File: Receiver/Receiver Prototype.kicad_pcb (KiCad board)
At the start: 4 copper layers, 145 x 50.8 mm, 108 parts, among them J1 Conn_01x02_Socket, J10 Conn_01x01, J11 Conn_Coaxial, J12 Conn_Coaxial, J13 Conn_Coaxial, J14 Conn_Coaxial, J15 Conn_01x01, J16 Conn_01x01, J17 Conn_01x02, J18 Conn_01x02, J19 Conn_01x01, J2 Conn_01x01, J20 Conn_01x01, J21 Conn_01x01, J22 Conn_01x01, J23 Conn_01x02, J24 Conn_01x02, J25 Conn_01x01, J26 Conn_01x03, J27 Conn_01x03, J28 Conn_01x02, J29 Conn_01x03, J3 Conn_01x01, J30 Conn_01x03, J4 Conn_Coaxial, J5 Conn_01x01, J6 Conn_01x02, J7 Conn_Coaxial, J8 Conn_Coaxial, J9 Conn_01x01, U1 OPA3692ID, U2 AD8692ARZ, U3 OPA692IDBVR, U4 LT3045EMSE-PBF, U5 AD607ARSZ, U6 LT3094EMSE-PBF

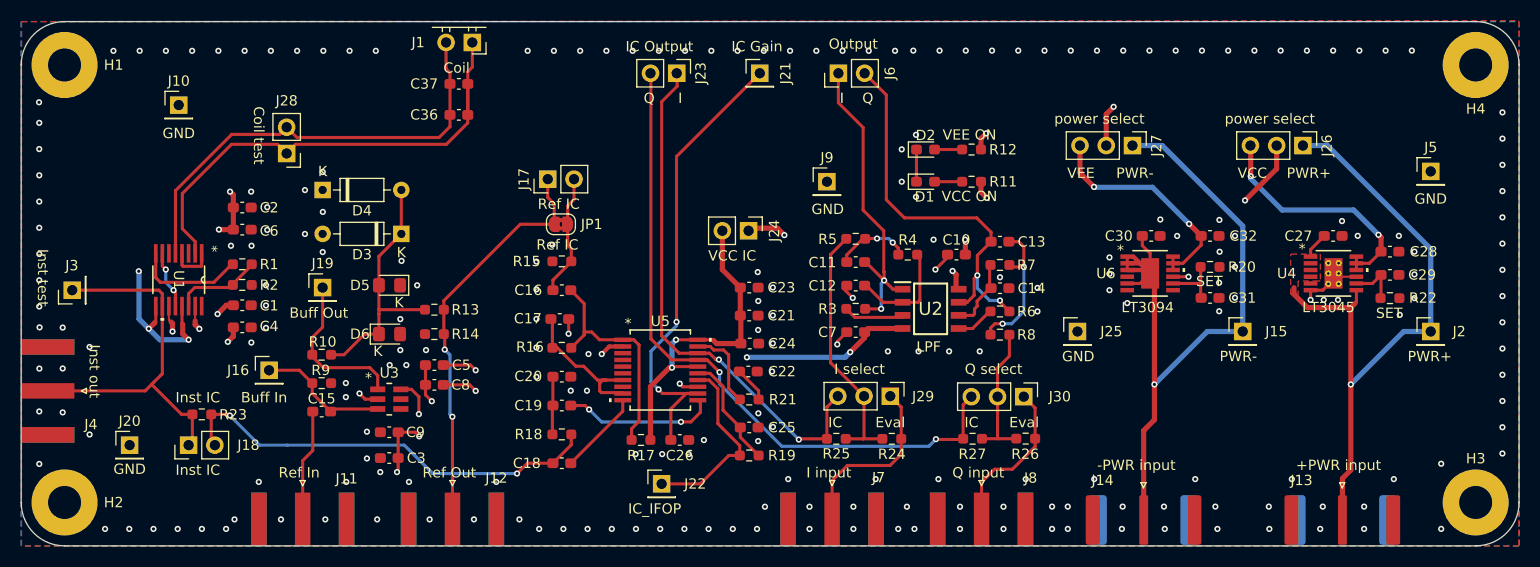
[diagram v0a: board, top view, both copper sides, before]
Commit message: Changed the Receiver layout as discussed on DR3
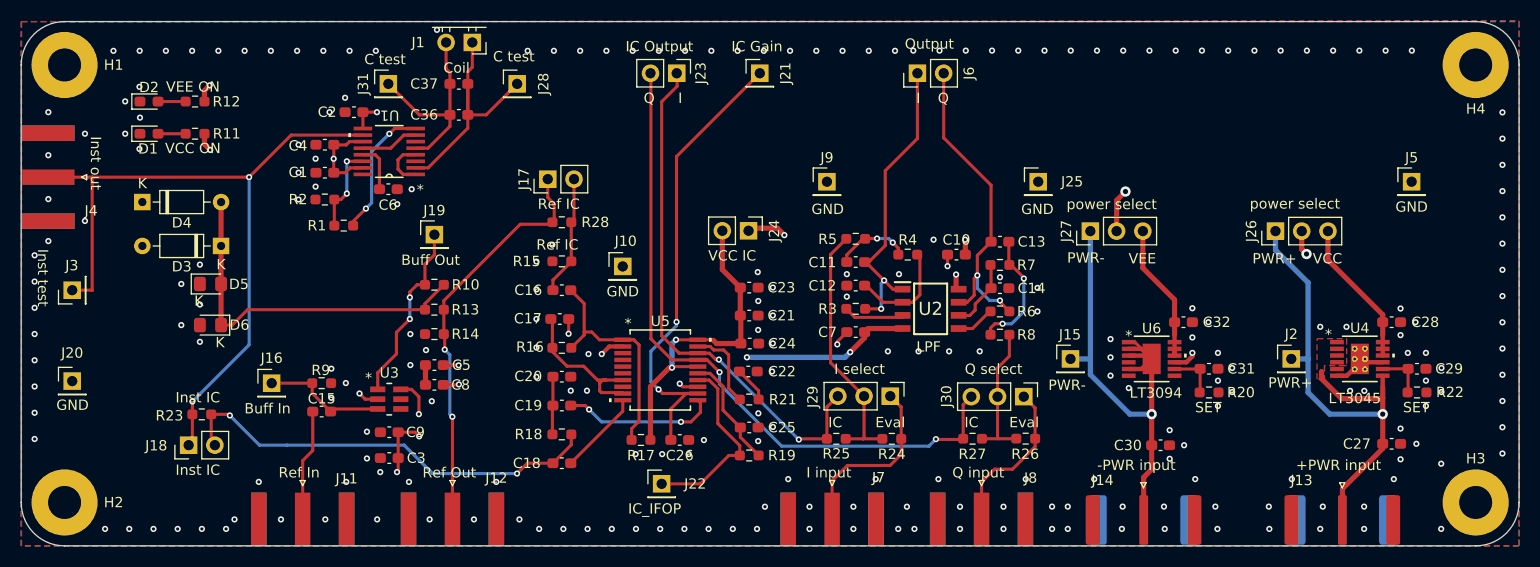
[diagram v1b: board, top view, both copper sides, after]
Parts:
- removed JP1: Jumper_2_Bridged, Jumper:SolderJumper-2_P1.3mm_Bridged2Bar_RoundedPad1.0x1.5mm
- added J31: Conn_01x01, Connector_PinHeader_2.54mm:PinHeader_1x01_P2.54mm_Vertical, F.Cu at (122.3, 56.0)
- added R28: R, Resistor_SMD:R_0603_1608Metric_Pad0.98x0.95mm_HandSolder, F.Cu at (139.1, 69.4)
- J28: value Conn_01x02 -> Conn_01x01; footprint Connector_PinHeader_2.54mm:PinHeader_1x02_P2.54mm_Vertical -> Connector_PinHeader_2.54mm:PinHeader_1x01_P2.54mm_Vertical
- moved R11 75.3 mm to (103.6, 60.9)
- moved R12 75.3 mm to (103.6, 57.7)
- moved D1 75.3 mm to (99.1, 60.9)
- moved D2 75.3 mm to (99.1, 57.7)
- moved J10 45.7 mm to (145.0, 73.7)
- moved U1 23.9 mm to (122.4, 62.6), turned to 180 degrees
- moved J28 23.3 mm to (134.8, 56.0), turned to 0 degrees
- moved C27 20.9 mm to (219.4, 90.9)
- moved J4 20.7 mm to (89.4, 65.1)
- moved C30 20.3 mm to (197.0, 91.0)
- moved C4 19.4 mm to (116.1, 61.9), turned to 180 degrees
- moved D3 17.5 mm to (106.1, 71.7)
- moved D4 17.5 mm to (98.5, 67.5)
- moved D6 17.4 mm to (105.1, 79.4), turned to 180 degrees
- moved D5 17.3 mm to (105.1, 75.4), turned to 0 degrees
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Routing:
- net /Inst_Out: track 79.1 -> 115.9 mm, vias 2 -> 4
- net /PWR-: track 75.0 -> 49.7 mm
- net /INB: track 44.3 -> 19.7 mm
- net /INA: track 48.5 -> 24.1 mm
- net VEE: track 52.8 -> 35.5 mm, vias 12 -> 8
- net /PWR+: track 66.4 -> 49.7 mm
- net Net-(D3-K): track 24.8 -> 35.4 mm
- net /VCC_In: track 23.7 -> 14.2 mm, vias 2 -> 0
- net /VEE_In: track 22.6 -> 14.0 mm, vias 2 -> 0
- net GND: track 27.4 -> 19.7 mm, vias 235 -> 240
- net /Q_Filter_Out: track 39.0 -> 31.7 mm
- net VCC: track 34.6 -> 29.2 mm, vias 12 -> 9
- net Net-(U1-INC+): track 10.6 -> 13.1 mm, vias 0 -> 2
- net /Buff_Out: track 15.5 -> 17.7 mm, vias 0 -> 2
- net Net-(C13-Pad2): track 13.8 -> 11.9 mm
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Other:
- board text added: "C test"
- board text removed: "Coil test"

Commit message: Fixed minor changes at Receiver
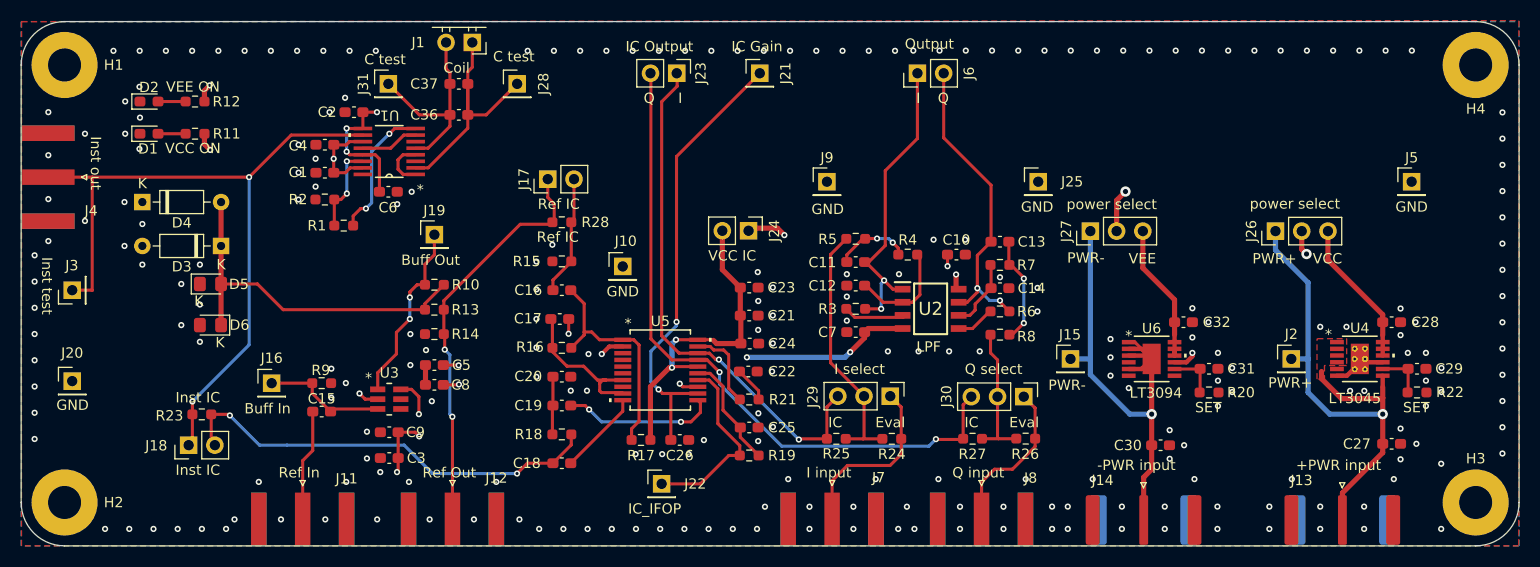
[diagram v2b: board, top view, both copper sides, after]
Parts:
- moved C6 0.25 mm to (122.3, 66.5)
- turned R8 to 180 degrees
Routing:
- net VEE: track 35.5 -> 41.3 mm, vias 8 -> 10
- net GND: track 19.7 -> 16.7 mm, vias 240 -> 243
- net /IC_Gain: track 45.5 -> 43.7 mm
- net Net-(C13-Pad2): track 11.9 -> 10.3 mm
- net /Q_Filter_Out: track 31.7 -> 30.5 mm
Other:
- board text added: "Receiver 1.0 2024-05-06"
- board text removed: "Receiver 1.0 2024-05-02"

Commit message: Modified Receiver layout
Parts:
- added C33: 0.1u, Capacitor_SMD:C_0603_1608Metric_Pad1.08x0.95mm_HandSolder, F.Cu at (139.1, 95.5)
- added J32: Conn_01x01, Connector_PinHeader_2.54mm:PinHeader_1x01_P2.54mm_Vertical, F.Cu at (131.7, 65.7)
- added J33: Conn_01x01, Connector_PinHeader_2.54mm:PinHeader_1x01_P2.54mm_Vertical, F.Cu at (112.0, 56.9)
- added J34: Conn_01x01, Connector_PinHeader_2.54mm:PinHeader_1x01_P2.54mm_Vertical, F.Cu at (111.2, 70.6)
- added J35: Conn_01x01, Connector_PinHeader_2.54mm:PinHeader_1x01_P2.54mm_Vertical, F.Cu at (99.0, 84.2)
- added J36: Conn_01x01, Connector_PinHeader_2.54mm:PinHeader_1x01_P2.54mm_Vertical, F.Cu at (145.0, 62.7)
- added J37: Conn_01x01, Connector_PinHeader_2.54mm:PinHeader_1x01_P2.54mm_Vertical, F.Cu at (112.4, 88.5)
- added R29: 0, Resistor_SMD:R_0603_1608Metric_Pad0.98x0.95mm_HandSolder, F.Cu at (156.1, 71.4)
- added R30: 0, Resistor_SMD:R_0603_1608Metric_Pad0.98x0.95mm_HandSolder, F.Cu at (190.3, 74.3)
- added R31: 0, Resistor_SMD:R_0603_1608Metric_Pad0.98x0.95mm_HandSolder, F.Cu at (195.3, 74.3)
- R3, R6: value 20k -> 0
- moved R3 40.8 mm to (208.2, 74.3), turned to 0 degrees
- moved R6 32.0 mm to (213.2, 74.4)
- moved R5 9.13 mm to (167.4, 80.2), turned to 180 degrees
- moved R4 5.96 mm to (167.4, 75.6)
- moved C7 5.63 mm to (172.9, 81.7), turned to 0 degrees
- moved C15 2.85 mm to (115.8, 84.9)
- moved J16 2.85 mm to (111.0, 82.2)
- moved R9 2.85 mm to (115.8, 82.2)
- moved J24 2.73 mm to (157.3, 67.5)
- moved C12 2.31 mm to (167.4, 77.9)
- moved C14 2.17 mm to (182.2, 77.9)
- moved R7 2.13 mm to (182.2, 75.6)
- moved C13 2.09 mm to (182.2, 73.3)
- moved C10 1.62 mm to (176.6, 74.0)
- moved R8 0.70 mm to (182.2, 80.2)
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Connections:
- C10 pad 1: VCC -> GND
- C10 pad 2: GND -> VCC
- C12 pad 1: Net-(U2--INA) -> Net-(U2-+INA)
- C14 pad 1: Net-(U2--INB) -> Net-(U2-+INB)
- C18 pad 1: /Inst_Out -> Net-(U5-GREF)
- D2 pad 1: GND -> Net-(D2-K)
- D2 pad 2: Net-(D2-A) -> GND
- R12 pad 2: Net-(D2-A) -> Net-(D2-K)
- R18 pad 2: /Inst_Out -> Net-(U5-GREF)
- R3 pad 1: /I_Filter_Out -> /PWR+
- R3 pad 2: Net-(U2-+INA) -> VCC
- R4 pad 2: Net-(U2--INA) -> Net-(U2-+INA)
- R6 pad 1: Net-(U2-+INB) -> VCC
- R6 pad 2: /Q_Filter_Out -> /VCC_In
- R7 pad 1: Net-(U2--INB) -> Net-(U2-+INB)
- U2 pad 2: Net-(U2--INA) -> /I_Filter_Out
- U2 pad 6: Net-(U2--INB) -> /Q_Filter_Out
- U5 pad 3: unconnected-(U5-PRUP-Pad3) -> /VCC_IC
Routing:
- net Net-(U5-GREF): track 15.0 -> 29.1 mm
- net /I_Filter_In: track 24.9 -> 13.8 mm
- net VCC: track 29.2 -> 40.2 mm, vias 9 -> 8
- net /PWR+: track 49.7 -> 39.4 mm, vias 1 -> 0
- net Net-(U2--INA): track 10.1 -> 0.00 mm
- net /VCC_IC: track 31.8 -> 40.3 mm, vias 2 -> 4
- net VEE: track 41.3 -> 49.0 mm
- net Net-(U2--INB): track 6.84 -> 0.00 mm
- net /Reference_In: track 10.8 -> 16.2 mm
- net /Inst_Out: track 115.9 -> 112.7 mm
- net Net-(U2-+INB): track 3.93 -> 6.90 mm
- net Net-(D2-K): track 0.00 -> 2.88 mm
- net /I_Filter_Out: track 30.1 -> 27.3 mm, vias 2 -> 0
- net Net-(D2-A): track 2.72 -> 0.00 mm
- net Net-(C13-Pad2): track 10.3 -> 7.91 mm, vias 2 -> 0
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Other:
- board text added: "Ref"

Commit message: Receiver ready for the second revision
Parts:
- removed D3, D4: 1N4148, Diode_THT:D_DO-35_SOD27_P7.62mm_Horizontal
- added J38: Conn_01x01, Connector_PinHeader_2.54mm:PinHeader_1x01_P2.54mm_Vertical, F.Cu at (201.7, 65.5)
- moved J34 14.3 mm to (102.7, 82.2)
- moved C26 13.4 mm to (151.2, 77.1)
- moved D5 11.0 mm to (115.9, 73.5)
- moved D6 10.9 mm to (115.8, 77.5)
- moved J36 7.68 mm to (141.2, 56.0)
- moved J35 7.30 mm to (96.4, 91.0)
- moved R16 3.33 mm to (139.1, 78.2)
- moved R21 2.69 mm to (157.1, 83.9)
- moved C17 2.66 mm to (139.0, 81.5), turned to 0 degrees
- moved C22 2.45 mm to (157.1, 86.3)
- moved J37 1.05 mm to (113.5, 88.5)
- moved J33 0.82 mm to (112.0, 56.0)
- moved J32 0.40 mm to (131.7, 65.2)
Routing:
- net Net-(D5-A): track 35.8 -> 16.3 mm
- net /IC_Gain: track 43.7 -> 37.8 mm
- net VCC: track 40.2 -> 37.3 mm
- net Net-(U5-FLTR): track 8.06 -> 5.24 mm
- net GND: track 16.4 -> 14.4 mm, vias 252 -> 271
- net Net-(U5-FDIN): track 22.3 -> 20.3 mm
- net Net-(U5-GREF): track 29.1 -> 27.9 mm
- net /Reference_In: track 16.2 -> 15.2 mm
- net /VCC_In: track 14.2 -> 15.0 mm
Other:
- board text added: "Receiver 2.0 2024-07-03"
- board text removed: "Receiver 1.0 2024-05-06"
